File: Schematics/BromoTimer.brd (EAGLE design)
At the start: 101.6 x 80 mm, 29 parts, among them IC1 PIC16F687, IC2 7805TV, K1 G2R2A, K2 G2R2A, Q1 BC548B, Q2 BC548B, Q3 BC548B, X1 AC_IN, X4 22-23-2041, X5 AC_OUT

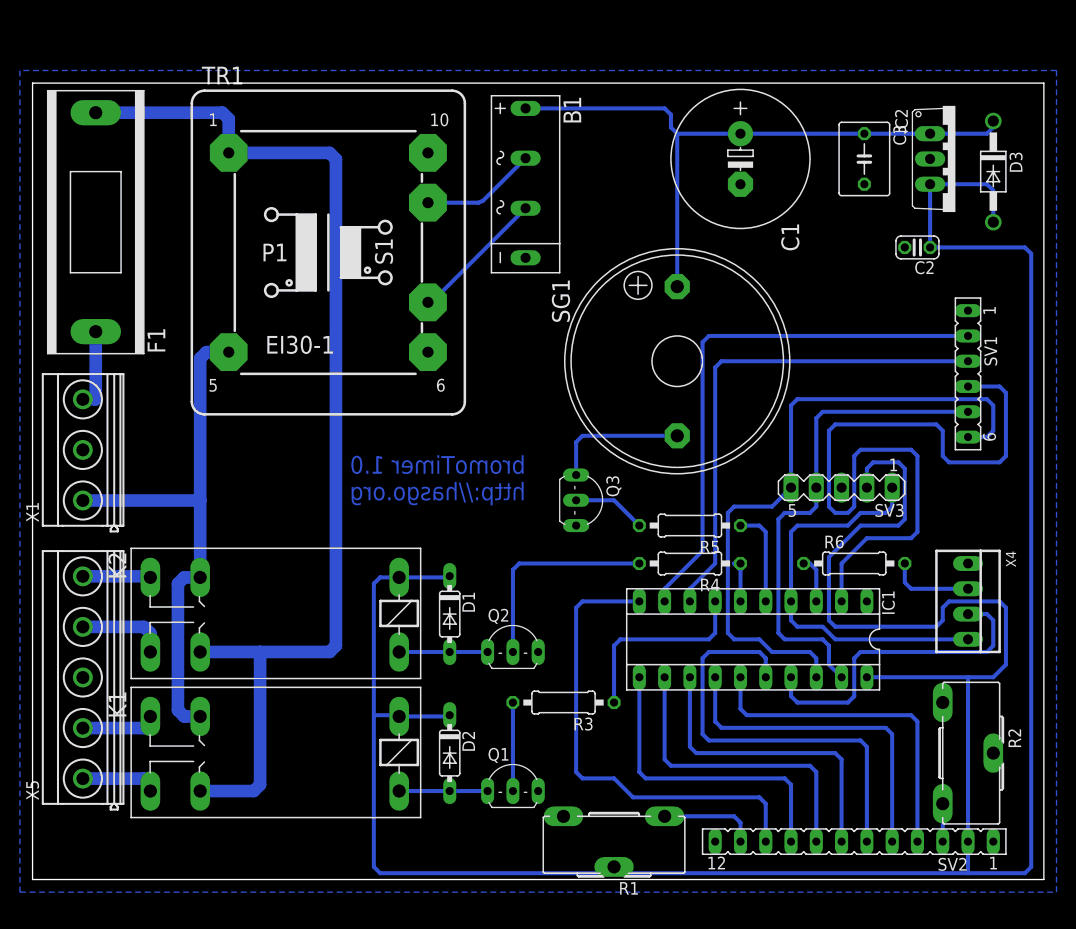
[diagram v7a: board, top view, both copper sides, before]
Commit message: New PCB prototype
The new PCB is a little taller and a lot less wide. It has extra space for the
7805 heatsink. Connector layout should be better, too.
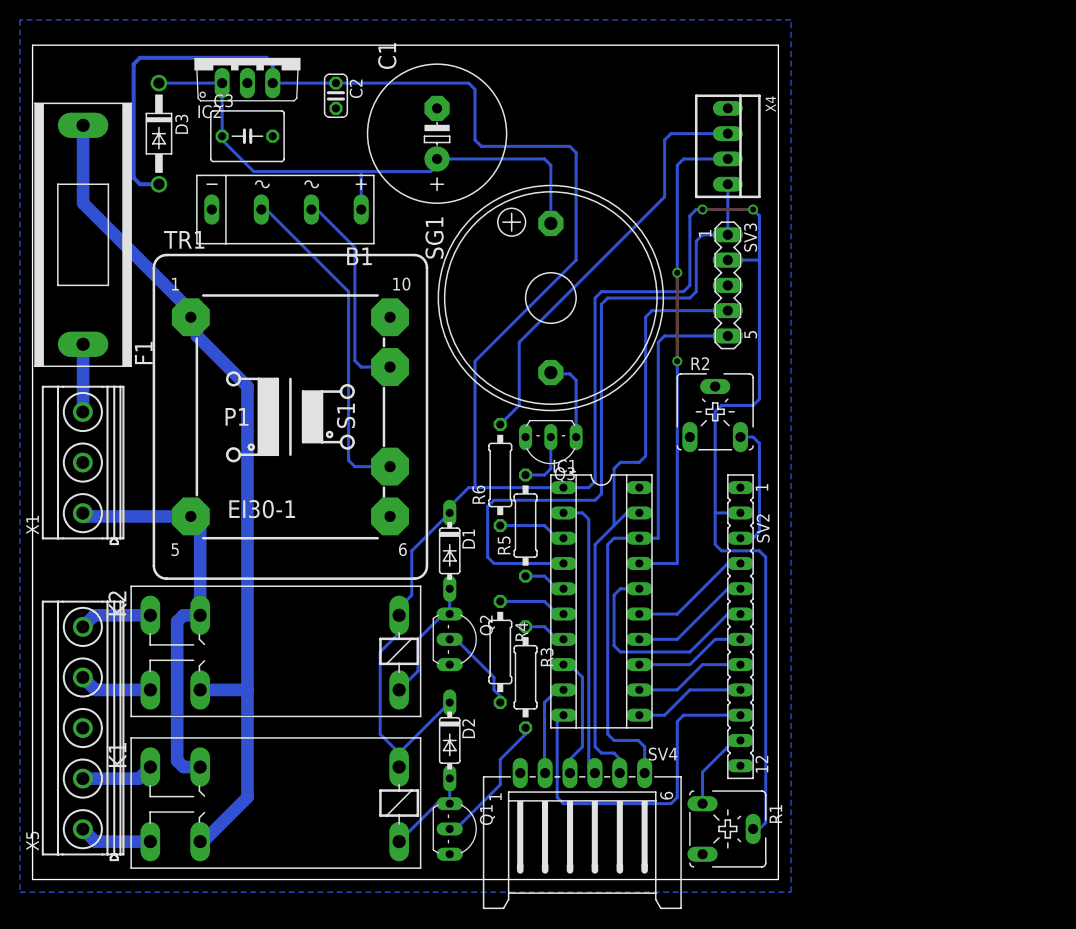
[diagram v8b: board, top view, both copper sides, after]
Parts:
- removed SV1: ENCODER, con-lsta:FE06
- added SV4: ENCODER, con-amp-mt:L06P
- B1: value (none) -> 500mA
- F1: value (none) -> 250V-500mA
- R1, R2: device pot:CA14H -> pot:CA6V
- R3, R4, R5: value (none) -> 1k
- moved D3 83.9 mm to (12.7, 74.9)
- moved IC2 71.8 mm to (21.6, 82.5), turned to 0 degrees
- moved C3 62.0 mm to (21.6, 74.7), turned to 0 degrees
- moved C2 60.4 mm to (30.5, 78.7), turned to 270 degrees
- moved X4 51.7 mm to (69.8, 73.7)
- moved R2 41.2 mm to (68.6, 47.0), turned to 0 degrees
- moved R6 36.7 mm to (47.0, 40.6), turned to 90 degrees
- moved C1 30.6 mm to (40.6, 74.9), turned to 90 degrees
- moved SV2 24.4 mm to (71.1, 25.4), turned to 270 degrees
- moved B1 24.3 mm to (25.4, 67.3), turned to 180 degrees
- moved SV3 23.3 mm to (69.8, 59.7), turned to 270 degrees
- moved R4 21.0 mm to (47.0, 22.9), turned to 270 degrees
- moved TR1 16.9 mm to (25.9, 46.5)
- moved R5 16.5 mm to (49.5, 35.6), turned to 90 degrees
- moved IC1 15.7 mm to (57.1, 27.9), turned to 270 degrees
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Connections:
- net +5V: now also IC1.1; no longer IC1.20
- net A: now also SV4.5; no longer SV1.5
- net B: now also SV4.6; no longer SV1.6
- net GND: now also IC1.20, SV4.1; no longer IC1.1, SV1.1
- net L1: now also SV4.2; no longer SV1.2
- net L2: now also SV4.3; no longer SV1.3
- net SW: now also SV4.4; no longer SV1.4
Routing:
- net SW: track 74.8 -> 28.6 mm
- net L1: track 54.5 -> 9.54 mm
- net L2: track 50.2 -> 12.6 mm
- net N$21: track 8.52 -> 42.0 mm
- net N$15: track 40.6 -> 67.6 mm
- net AC2: track 110.4 -> 85.7 mm
- net RW: track 33.5 -> 12.3 mm
- net RS: track 33.5 -> 12.3 mm
- net EN: track 43.0 -> 22.4 mm
- net N$2: track 13.7 -> 33.6 mm
- net B2: track 31.0 -> 11.2 mm
- net B1: track 31.0 -> 11.2 mm
- net B0: track 31.0 -> 11.2 mm
- net N$13: track 32.4 -> 49.2 mm, vias 0 -> 2
- net N$16: track 19.6 -> 4.34 mm
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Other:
- board size 101.6 x 80 mm -> 74.9 x 83.8 mm
- board text removed: "bromoTimer 1.0 http://hasgo.org"
